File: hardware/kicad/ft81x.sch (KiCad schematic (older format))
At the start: 7 parts, among them U6 FT813, X1 YSX321SL

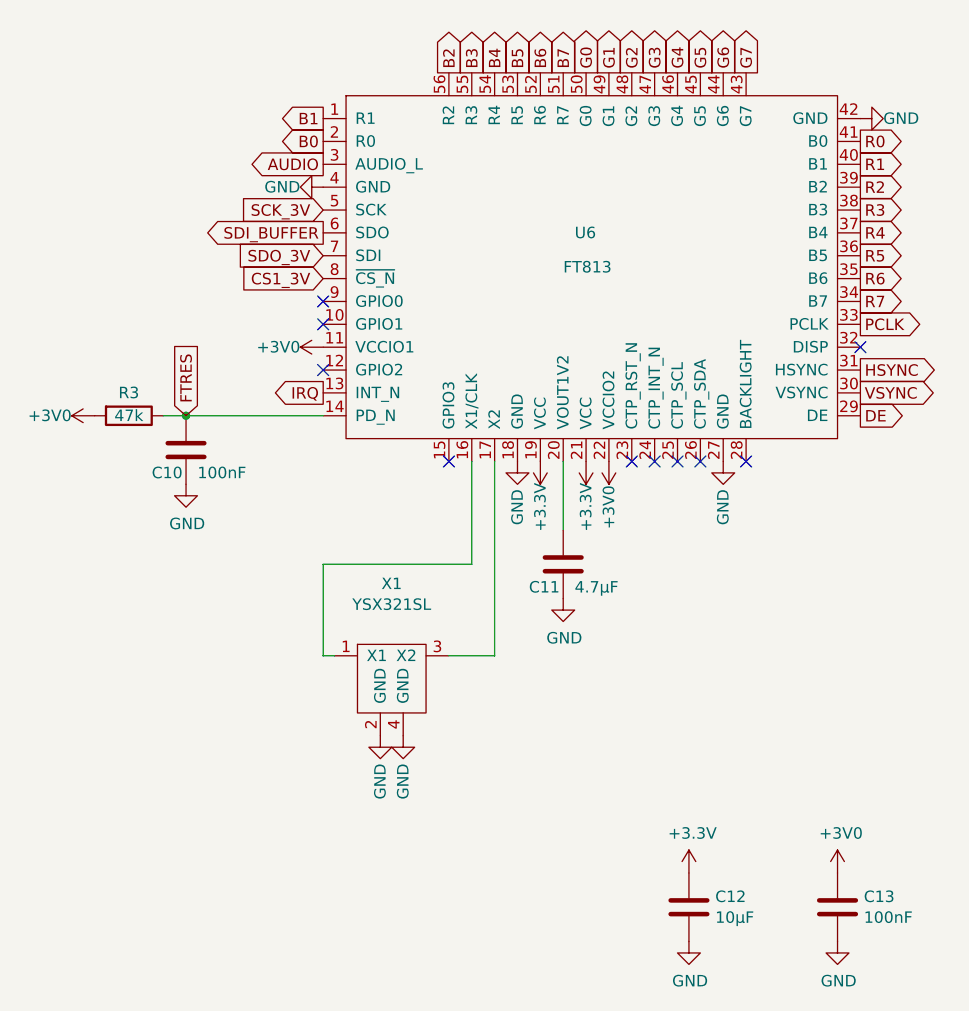
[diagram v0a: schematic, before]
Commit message: Rework display reset circuit and improve 3v power supply
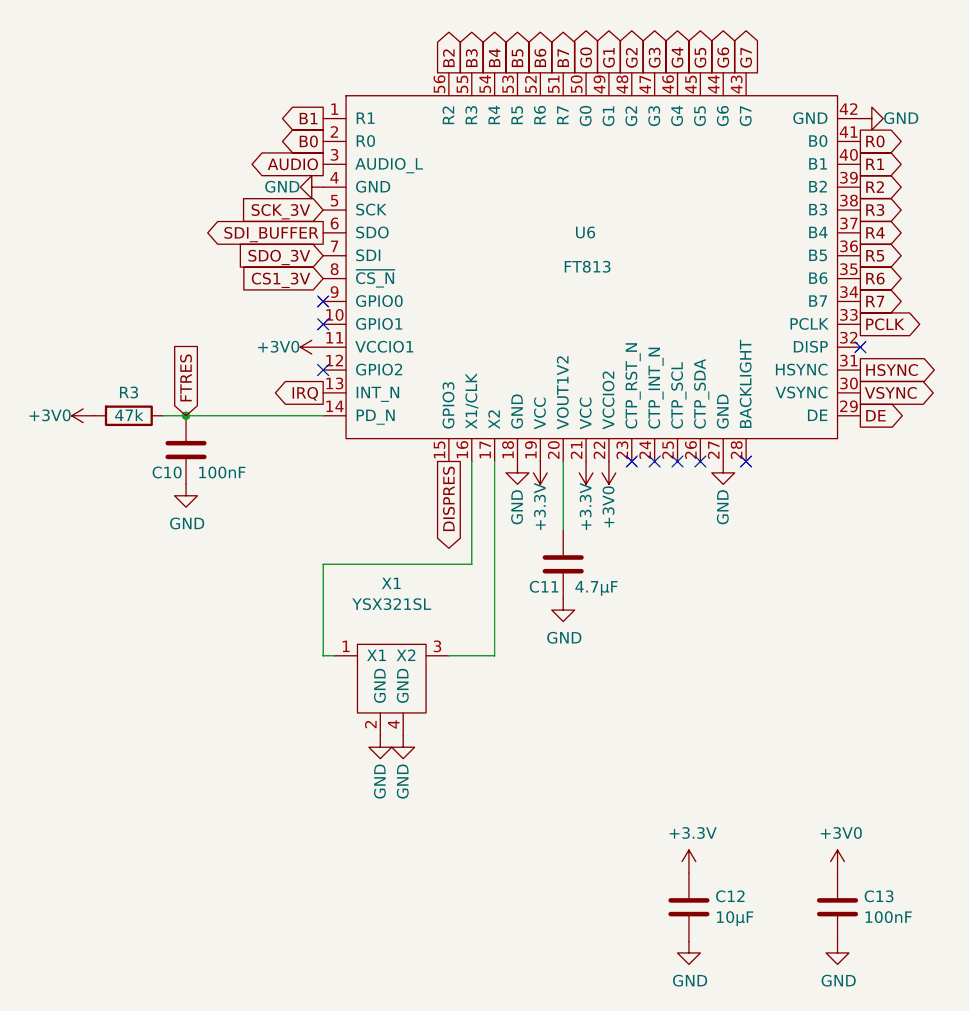
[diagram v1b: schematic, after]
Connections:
- net DISPRES: now reaches U6.15 (GPIO3)
- no-connect marks 10 -> 9
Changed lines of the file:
@@
 NoConn ~ 6600 3100
 NoConn ~ 7100 2600
-NoConn ~ 5300 3100
 NoConn ~ 4750 2700
 NoConn ~ 4750 2500
@@
 Text GLabel 4750 2800 0    50   Output ~ 0
 IRQ
+Text GLabel 5300 3100 3    50   Output ~ 0
+DISPRES
 $EndSCHEMATC

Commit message: Add digikey bom alternative
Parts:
- C10, C13: DigiKey (none) -> 311-1335-1-ND
- C11: DigiKey (none) -> 1276-1045-1-ND
- C12: DigiKey (none) -> 478-10766-1-ND
- R3: DigiKey (none) -> 311-47KGRCT-ND
- U6: DigiKey (none) -> FT812Q-T
- X1: DigiKey (none) -> RH100-12.000-12-1010-EXT-TR
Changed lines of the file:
@@
 F 2 "Package_DFN_QFN:QFN-56-1EP_8x8mm_P0.5mm_EP5.6x5.6mm_HandSolder" H 5900 2250 50  0001 C CNN
 F 3 "" H 5900 2250 50  0001 C CNN
+F 4 "FT812Q-T" H 5900 2250 50  0001 C CNN "DigiKey"
 	1    5900 2250
 	1    0    0    -1
@@
 F 3 "~" H 3900 2900 50  0001 C CNN
 F 4 "C25819 " H 3900 2900 50  0001 C CNN "LCSC"
+F 5 "311-47KGRCT-ND" H 3900 2900 50  0001 C CNN "DigiKey"
 	1    3900 2900
 	0    1    1    0
@@
 F 3 "~" H 4150 3050 50  0001 C CNN
 F 4 "C14663" H 4150 3050 50  0001 C CNN "LCSC"
+F 5 "311-1335-1-ND" H 4150 3050 50  0001 C CNN "DigiKey"
 	1    4150 3050
 	1    0    0    -1
@@
 F 3 "~" H 5800 3550 50  0001 C CNN
 F 4 "C19666" H 5800 3550 50  0001 C CNN "LCSC"
+F 5 "1276-1045-1-ND" H 5800 3550 50  0001 C CNN "DigiKey"
 	1    5800 3550
 	1    0    0    -1
@@
 F 3 "" H 5000 4000 50  0001 C CNN
 F 4 "C9002" H 5050 4000 50  0001 C CNN "LCSC"
+F 5 "RH100-12.000-12-1010-EXT-TR" H 5050 4000 50  0001 C CNN "DigiKey"
 	1    5050 4000
 	1    0    0    -1
@@
 F 3 "~" H 6350 5050 50  0001 C CNN
 F 4 "C19702" H 6350 5050 50  0001 C CNN "LCSC"
+F 5 "478-10766-1-ND" H 6350 5050 50  0001 C CNN "DigiKey"
 	1    6350 5050
 	1    0    0    -1
@@
 F 3 "~" H 7000 5050 50  0001 C CNN
 F 4 "C14663" H 7000 5050 50  0001 C CNN "LCSC"
+F 5 "311-1335-1-ND" H 7000 5050 50  0001 C CNN "DigiKey"
 	1    7000 5050
 	1    0    0    -1

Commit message: Update footprints for machine assembly
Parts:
- U6: footprint Package_DFN_QFN:QFN-56-1EP_8x8mm_P0.5mm_EP5.6x5.6mm_HandSolder -> Package_DFN_QFN:QFN-56-1EP_8x8mm_P0.5mm_EP5.6x5.6mm
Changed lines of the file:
@@
 F 0 "U6" H 5850 2400 50  0000 L CNN
 F 1 "FT813" H 5800 2250 50  0000 L CNN
-F 2 "Package_DFN_QFN:QFN-56-1EP_8x8mm_P0.5mm_EP5.6x5.6mm_HandSolder" H 5900 2250 50  0001 C CNN
+F 2 "Package_DFN_QFN:QFN-56-1EP_8x8mm_P0.5mm_EP5.6x5.6mm" H 5900 2250 50  0001 C CNN
 F 3 "" H 5900 2250 50  0001 C CNN
 F 4 "FT812Q-T" H 5900 2250 50  0001 C CNN "DigiKey"

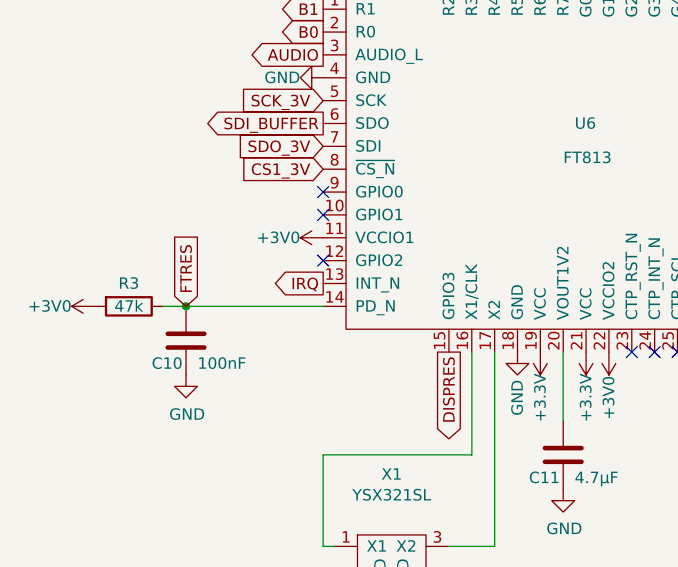
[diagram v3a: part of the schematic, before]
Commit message: Clean up board and expose less debug signals
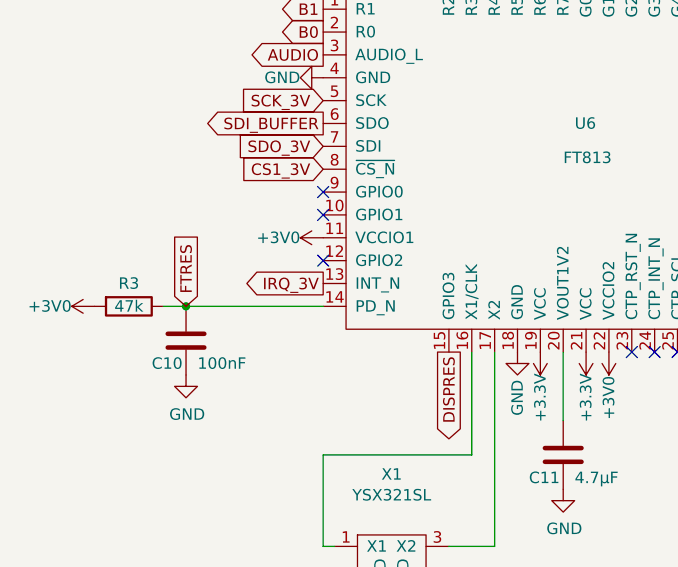
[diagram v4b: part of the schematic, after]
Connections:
- net IRQ renamed IRQ_3V
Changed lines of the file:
@@
 $EndDescr
 $Comp
-L driver-board-rescue:FT813-driver-board-driver-board-rescue U6
+L driver-board-rescue:FT813-driver-board-driver-board-rescue U?
 U 1 1 5F0268C1
 P 5900 2250
-AR Path="/5F0268C1" Ref="U6"  Part="1"
+AR Path="/5F0268C1" Ref="U?"  Part="1"
 AR Path="/5F022188/5F0268C1" Ref="U6"  Part="1"
 F 0 "U6" H 5850 2400 50  0000 L CNN
@@
 CS1_3V
 $Comp
-L power:GND #PWR034
+L power:GND #PWR036
 U 1 1 5F02B6C5
 P 4750 1900
-F 0 "#PWR034" H 4750 1650 50  0001 C CNN
+F 0 "#PWR036" H 4750 1650 50  0001 C CNN
 F 1 "GND" V 4750 1800 50  0000 R CNN
 F 2 "" H 4750 1900 50  0001 C CNN
@@
 $EndComp
 $Comp
-L power:+3.3V #PWR038
+L power:+3.3V #PWR040
 U 1 1 5F02BC5F
 P 5700 3100
-F 0 "#PWR038" H 5700 2950 50  0001 C CNN
+F 0 "#PWR040" H 5700 2950 50  0001 C CNN
 F 1 "+3.3V" V 5700 3300 50  0000 C CNN
 F 2 "" H 5700 3100 50  0001 C CNN
@@
 $EndComp
 $Comp
-L power:+3.3V #PWR039
+L power:+3.3V #PWR041
 U 1 1 5F02BEAA
 P 5900 3100
-F 0 "#PWR039" H 5900 2950 50  0001 C CNN
+F 0 "#PWR041" H 5900 2950 50  0001 C CNN
 F 1 "+3.3V" V 5900 3300 50  0000 C CNN
 F 2 "" H 5900 3100 50  0001 C CNN
@@
 $EndComp
 $Comp
-L power:GND #PWR041
+L power:GND #PWR043
 U 1 1 5F02C6DE
 P 6500 3100
-F 0 "#PWR041" H 6500 2850 50  0001 C CNN
+F 0 "#PWR043" H 6500 2850 50  0001 C CNN
 F 1 "GND" V 6500 2900 50  0000 C CNN
 F 2 "" H 6500 3100 50  0001 C CNN
@@
 $EndComp
 $Comp
-L power:GND #PWR033
+L power:GND #PWR035
 U 1 1 5F02CB8C
 P 7100 1600
-F 0 "#PWR033" H 7100 1350 50  0001 C CNN
+F 0 "#PWR035" H 7100 1350 50  0001 C CNN
 F 1 "GND" V 7100 1500 50  0000 R CNN
 F 2 "" H 7100 1600 50  0001 C CNN
@@
 	4150 2900 4050 2900
 $Comp
-L power:GND #PWR042
+L power:GND #PWR044
 U 1 1 5F02F445
 P 4150 3200
-F 0 "#PWR042" H 4150 2950 50  0001 C CNN
+F 0 "#PWR044" H 4150 2950 50  0001 C CNN
 F 1 "GND" H 4155 3027 50  0000 C CNN
 F 2 "" H 4150 3200 50  0001 C CNN
@@
 	5800 3100 5800 3400
 $Comp
-L power:GND #PWR043
+L power:GND #PWR045
 U 1 1 5F033AAC
 P 5800 3700
-F 0 "#PWR043" H 5800 3450 50  0001 C CNN
+F 0 "#PWR045" H 5800 3450 50  0001 C CNN
 F 1 "GND" H 5805 3527 50  0000 C CNN
 F 2 "" H 5800 3700 50  0001 C CNN
@@
 $EndComp
 $Comp
-L power:GND #PWR044
+L power:GND #PWR046
 U 1 1 5F03AD9F
 P 5000 4300
-F 0 "#PWR044" H 5000 4050 50  0001 C CNN
+F 0 "#PWR046" H 5000 4050 50  0001 C CNN
 F 1 "GND" V 5000 4100 50  0000 C CNN
 F 2 "" H 5000 4300 50  0001 C CNN
@@
 $EndComp
 $Comp
-L power:GND #PWR045
+L power:GND #PWR047
 U 1 1 5F03AF97
 P 5100 4300
-F 0 "#PWR045" H 5100 4050 50  0001 C CNN
+F 0 "#PWR047" H 5100 4050 50  0001 C CNN
 F 1 "GND" V 5100 4100 50  0000 C CNN
 F 2 "" H 5100 4300 50  0001 C CNN
@@
 	4750 3950 4800 3950
 $Comp
-L power:+3V0 #PWR036
+L power:+3V0 #PWR038
 U 1 1 5F0403D2
 P 3750 2900
-F 0 "#PWR036" H 3750 2750 50  0001 C CNN
+F 0 "#PWR038" H 3750 2750 50  0001 C CNN
 F 1 "+3V0" V 3750 3000 50  0000 L CNN
 F 2 "" H 3750 2900 50  0001 C CNN
@@
 $EndComp
 $Comp
-L power:+3V0 #PWR035
+L power:+3V0 #PWR037
 U 1 1 5F040E18
 P 4750 2600
-F 0 "#PWR035" H 4750 2450 50  0001 C CNN
+F 0 "#PWR037" H 4750 2450 50  0001 C CNN
 F 1 "+3V0" V 4750 2700 50  0000 L CNN
 F 2 "" H 4750 2600 50  0001 C CNN
@@
 $EndComp
 $Comp
-L power:+3V0 #PWR040
+L power:+3V0 #PWR042
 U 1 1 5F041F56
 P 6000 3100
-F 0 "#PWR040" H 6000 2950 50  0001 C CNN
+F 0 "#PWR042" H 6000 2950 50  0001 C CNN
 F 1 "+3V0" V 6000 3300 50  0000 C CNN
 F 2 "" H 6000 3100 50  0001 C CNN
@@
 NoConn ~ 4750 2400
 $Comp
-L power:GND #PWR037
+L power:GND #PWR039
 U 1 1 5F095769
 P 5600 3100
-F 0 "#PWR037" H 5600 2850 50  0001 C CNN
+F 0 "#PWR039" H 5600 2850 50  0001 C CNN
 F 1 "GND" V 5600 2900 50  0000 C CNN
 F 2 "" H 5600 3100 50  0001 C CNN
@@
 $EndComp
 $Comp
-L power:+3.3V #PWR046
+L power:+3.3V #PWR048
 U 1 1 5F0BB418
 P 6350 4900
-F 0 "#PWR046" H 6350 4750 50  0001 C CNN
+F 0 "#PWR048" H 6350 4750 50  0001 C CNN
 F 1 "+3.3V" H 6365 5073 50  0000 C CNN
 F 2 "" H 6350 4900 50  0001 C CNN
@@
 $EndComp
 $Comp
-L power:GND #PWR048
+L power:GND #PWR050
 U 1 1 5F0BBD7E
 P 6350 5200
-F 0 "#PWR048" H 6350 4950 50  0001 C CNN
+F 0 "#PWR050" H 6350 4950 50  0001 C CNN
 F 1 "GND" H 6355 5027 50  0000 C CNN
 F 2 "" H 6350 5200 50  0001 C CNN
@@
 $EndComp
 $Comp
-L power:GND #PWR049
+L power:GND #PWR051
 U 1 1 5F0CC6D1
 P 7000 5200
-F 0 "#PWR049" H 7000 4950 50  0001 C CNN
+F 0 "#PWR051" H 7000 4950 50  0001 C CNN
 F 1 "GND" H 7005 5027 50  0000 C CNN
 F 2 "" H 7000 5200 50  0001 C CNN
@@
 $EndComp
 $Comp
-L power:+3V0 #PWR047
+L power:+3V0 #PWR049
 U 1 1 5F0CC952
 P 7000 4900
-F 0 "#PWR047" H 7000 4750 50  0001 C CNN
+F 0 "#PWR049" H 7000 4750 50  0001 C CNN
 F 1 "+3V0" H 7015 5073 50  0000 C CNN
 F 2 "" H 7000 4900 50  0001 C CNN
@@
 FTRES
 Text GLabel 4750 2800 0    50   Output ~ 0
-IRQ
+IRQ_3V
 Text GLabel 5300 3100 3    50   Output ~ 0
 DISPRES

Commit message: Update BOM
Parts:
- C10, C13: Description (none) -> CAP CER 0.1UF 16V X7R 0603; DigiKey 311-1335-1-ND -> (none); Manufacturer (none) -> Yageo; Mfg Part # (none) -> CC0603KPX7R7BB104
- C11: Description (none) -> CAP CER 4.7UF 6.3V X5R 0603; DigiKey 1276-1045-1-ND -> (none); Manufacturer (none) -> Samsung Electro-Mechanics; Mfg Part # (none) -> CL10A475KQ8NNNC
- C12: Description (none) -> CAP CER 10UF 10V X5R 0603; DigiKey 478-10766-1-ND -> (none); Manufacturer (none) -> AVX Corporation; Mfg Part # (none) -> 0603ZD106KAT2A
- R3: Description (none) -> RES SMD 47K OHM 5% 1/10W 0603; DigiKey 311-47KGRCT-ND -> (none); Manufacturer (none) -> Yageo; Mfg Part # (none) -> RC0603JR-0747KL
- U6: Description (none) -> IC VIDEO GRAPHIC CNTL 56VQFN; DigiKey FT812Q-T -> (none); Manufacturer (none) -> Bridgetek Pte Ltd.; Mfg Part # (none) -> FT812Q-T
- X1: Description (none) -> XTAL 12MHZ 12PF SMD; DigiKey RH100-12.000-12-1010-EXT-TR -> (none); Manufacturer (none) -> Raltron Electronics; Mfg Part # (none) -> RH100-12.000-12-1010-EXT-TR
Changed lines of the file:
@@
 F 2 "Package_DFN_QFN:QFN-56-1EP_8x8mm_P0.5mm_EP5.6x5.6mm" H 5900 2250 50  0001 C CNN
 F 3 "" H 5900 2250 50  0001 C CNN
-F 4 "FT812Q-T" H 5900 2250 50  0001 C CNN "DigiKey"
+F 4 "Bridgetek Pte Ltd." H 5900 2250 50  0001 C CNN "Manufacturer"
+F 5 "IC VIDEO GRAPHIC CNTL 56VQFN" H 5900 2250 50  0001 C CNN "Description"
+F 6 "FT812Q-T" H 5900 2250 50  0001 C CNN "Mfg Part #"
 	1    5900 2250
 	1    0    0    -1
@@
 F 3 "~" H 3900 2900 50  0001 C CNN
 F 4 "C25819 " H 3900 2900 50  0001 C CNN "LCSC"
-F 5 "311-47KGRCT-ND" H 3900 2900 50  0001 C CNN "DigiKey"
+F 5 "" H 3900 2900 50  0001 C CNN "DigiKey"
+F 6 "RC0603JR-0747KL" H 3900 2900 50  0001 C CNN "Mfg Part #"
+F 7 "RES SMD 47K OHM 5% 1/10W 0603" H 3900 2900 50  0001 C CNN "Description"
+F 8 "Yageo" H 3900 2900 50  0001 C CNN "Manufacturer"
 	1    3900 2900
 	0    1    1    0
@@
 F 3 "~" H 4150 3050 50  0001 C CNN
 F 4 "C14663" H 4150 3050 50  0001 C CNN "LCSC"
-F 5 "311-1335-1-ND" H 4150 3050 50  0001 C CNN "DigiKey"
+F 5 "" H 4150 3050 50  0001 C CNN "DigiKey"
+F 6 "CC0603KPX7R7BB104" H 4150 3050 50  0001 C CNN "Mfg Part #"
+F 7 "CAP CER 0.1UF 16V X7R 0603" H 4150 3050 50  0001 C CNN "Description"
+F 8 "Yageo" H 4150 3050 50  0001 C CNN "Manufacturer"
 	1    4150 3050
 	1    0    0    -1
@@
 F 3 "~" H 5800 3550 50  0001 C CNN
 F 4 "C19666" H 5800 3550 50  0001 C CNN "LCSC"
-F 5 "1276-1045-1-ND" H 5800 3550 50  0001 C CNN "DigiKey"
+F 5 "" H 5800 3550 50  0001 C CNN "DigiKey"
+F 6 "CL10A475KQ8NNNC" H 5800 3550 50  0001 C CNN "Mfg Part #"
+F 7 "CAP CER 4.7UF 6.3V X5R 0603" H 5800 3550 50  0001 C CNN "Description"
+F 8 "Samsung Electro-Mechanics" H 5800 3550 50  0001 C CNN "Manufacturer"
 	1    5800 3550
 	1    0    0    -1
@@
 F 3 "" H 5000 4000 50  0001 C CNN
 F 4 "C9002" H 5050 4000 50  0001 C CNN "LCSC"
-F 5 "RH100-12.000-12-1010-EXT-TR" H 5050 4000 50  0001 C CNN "DigiKey"
+F 5 "" H 5050 4000 50  0001 C CNN "DigiKey"
+F 6 "RH100-12.000-12-1010-EXT-TR" H 5050 4000 50  0001 C CNN "Mfg Part #"
+F 7 "XTAL 12MHZ 12PF SMD" H 5050 4000 50  0001 C CNN "Description"
+F 8 "Raltron Electronics" H 5050 4000 50  0001 C CNN "Manufacturer"
 	1    5050 4000
 	1    0    0    -1
@@
 F 3 "~" H 6350 5050 50  0001 C CNN
 F 4 "C19702" H 6350 5050 50  0001 C CNN "LCSC"
-F 5 "478-10766-1-ND" H 6350 5050 50  0001 C CNN "DigiKey"
+F 5 "" H 6350 5050 50  0001 C CNN "DigiKey"
+F 6 "0603ZD106KAT2A" H 6350 5050 50  0001 C CNN "Mfg Part #"
+F 7 "CAP CER 10UF 10V X5R 0603" H 6350 5050 50  0001 C CNN "Description"
+F 8 "AVX Corporation" H 6350 5050 50  0001 C CNN "Manufacturer"
 	1    6350 5050
 	1    0    0    -1
@@
 F 3 "~" H 7000 5050 50  0001 C CNN
 F 4 "C14663" H 7000 5050 50  0001 C CNN "LCSC"
-F 5 "311-1335-1-ND" H 7000 5050 50  0001 C CNN "DigiKey"
+F 5 "" H 7000 5050 50  0001 C CNN "DigiKey"
+F 6 "CC0603KPX7R7BB104" H 7000 5050 50  0001 C CNN "Mfg Part #"
+F 7 "CAP CER 0.1UF 16V X7R 0603" H 7000 5050 50  0001 C CNN "Description"
+F 8 "Yageo" H 7000 5050 50  0001 C CNN "Manufacturer"
 	1    7000 5050
 	1    0    0    -1
